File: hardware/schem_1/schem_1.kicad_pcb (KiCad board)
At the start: 2 copper layers, 100 x 40 mm, 68 parts, among them J1 OV7670_Conn_01x24_MountingPin, J2 Micro_SD_Card, J3 USB_B_Mini, J4 Conn_01x03_Female, Q1 NDS332P, SW1 BTN_BOOT, SW2 ESP32_RESET, SW4 DOWN, SW5 UP, SW6 OK, U1 ESP32-S2-WROVER-JC, U2 XC6210B332MR, U5 XC6206-2.8V, U6 XC6206-1.2V, U7 128x32_OLED_SSD1306, U8 MCP23017_SO

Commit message: update footprint for OLED display (no longer using ffc connector)
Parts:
- added R5: 0R DNF, Resistor_SMD:R_0603_1608Metric, F.Cu at (-127.0, -96.1)
- U7: footprint Connector_FFC-FPC:TE_1-1734839-4_1x14-1MP_P0.5mm_Horizontal -> kicad_lib:ER-OLED0.91-7W_SSD1306
- moved C22 458.4 mm to (-259.5, -106.7)
- moved C21 457.4 mm to (-276.3, -46.2)
- moved C17 454.4 mm to (-255.3, -107.0)
- moved C19 446.8 mm to (-247.3, -107.0)
- moved C18 445.1 mm to (-251.3, -107.0)
- moved C20 441.1 mm to (-243.3, -107.0)
- moved R21 441.1 mm to (-239.3, -107.0)
- moved R20 425.2 mm to (-235.3, -107.0)
- moved U7 395.4 mm to (-208.0, -82.0), turned to 90 degrees
- moved C25 380.4 mm to (-239.1, -7.35)
- moved C6 380.4 mm to (-228.2, -23.5)
- moved J2 380.4 mm to (-237.6, -25.3)
- moved R1 380.4 mm to (-228.2, -21.0)
- moved R11 380.4 mm to (-228.2, -18.5)
- moved R12 380.4 mm to (-232.3, -13.4)
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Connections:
- J3 pad 3: Net-(J3-Pad2) -> Net-(J3-Pad3)

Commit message: update footprints for 24way connector, 3D models. add new connector to connect the two PCB's
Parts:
- added H1: MountingHole, MountingHole:MountingHole_2mm, F.Cu at (119.6, 27.0)
- added H2: MountingHole, MountingHole:MountingHole_2mm, F.Cu at (147.6, 27.0)
- added H3: MountingHole, MountingHole:MountingHole_2mm, F.Cu at (147.6, -0.96)
- added H4: MountingHole, MountingHole:MountingHole_2mm, F.Cu at (119.6, -0.96)
- added J5: UJ2-MBH-1-SMT, UJ2-MBH-1-SMT:CUI_UJ2-MBH-1-SMT, F.Cu at (93.1, 4.74)
- added R10: 3.3k, Resistor_SMD:R_0603_1608Metric, F.Cu at (64.0, 15.9)
- added R28: 3.3k, Resistor_SMD:R_0603_1608Metric, F.Cu at (64.0, 31.6)
- added R29: 3.3k, Resistor_SMD:R_0603_1608Metric, F.Cu at (64.0, 27.6)
- added R9: 3.3k, Resistor_SMD:R_0603_1608Metric, F.Cu at (64.0, 19.9)
- C10, C11, C12, C15, C16, C17, C18, C19, C2, C20, C21, C22, C23, C24, C3, C4, C5, C8, C9, D1, D2, D3, D4, J4, R1, R16, R17, R18, R19, R20, R21, R22, R23, R24, R25, R3, R4, R6, R7, U2, U6, U8: moved to B.Cu
- J3: value USB_B_Mini -> PCB_CONNECTOR; footprint kicad_lib:USB_Mini_B_Female_UJ2-MBH-1-SMT-TR-JC -> Connector_FFC-FPC:TE_2-1734839-4_1x24-1MP_P0.5mm_Horizontal; moved to B.Cu
- R26, R27: value 10k -> 3.3k
- R5: value 0R DNF -> 0R; moved to B.Cu
- SW1: footprint Digikey:Switch_Tactile_SMD_4.5x4.5mm_TL3315NF160Q -> kicad_lib:JC_Switch_TL6330
- SW2: footprint Digikey:Switch_Tactile_SMD_4.5x4.5mm_TL3315NF160Q -> kicad_lib:JC_Switch_TL6330; moved to B.Cu
- SW4, SW5, SW6: footprint Digikey:Switch_Tactile_SMD_6x6mm_PTS645 -> kicad_lib:JC_Switch_TL6330
- moved SW2 408.4 mm to (166.6, -5.65), turned to 180 degrees
- moved U1 397.6 mm to (134.9, 11.5), turned to 180 degrees
- moved R2 396.5 mm to (171.7, -0.57)
- moved SW1 396.3 mm to (168.8, -6.03)
- moved C6 392.3 mm to (163.5, -1.33)
- moved C26 390.7 mm to (147.1, 18.5)
- moved R27 390.6 mm to (147.1, 12.0), turned to 180 degrees
- moved R8 388.7 mm to (163.8, 1.97)
- moved C25 387.1 mm to (147.1, 20.1)
- moved C15 363.9 mm to (208.7, 20.1), turned to 270 degrees
- moved C21 362.6 mm to (82.9, 2.95), turned to 90 degrees
- moved C1 362.5 mm to (147.3, 21.9)
- moved U6 359.1 mm to (206.2, 8.60)
- moved J1 357.6 mm to (119.0, 11.0), turned to 90 degrees
- moved C22 357.2 mm to (73.1, 23.5)
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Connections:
- J3 pad 1: /GPIO Expander/Vusb -> Net-(J3-Pad1)
- J3 pad 5: GND -> Net-(J3-Pad5)
- J3 pad 6: GND -> Net-(J3-Pad6)
- R5 pad 1: Net-(J3-Pad2) -> Net-(J5-Pad2)
- R5 pad 2: Net-(J3-Pad3) -> Net-(J5-Pad3)
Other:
- board size 100 x 40 mm -> 80.4 x 34.2 mm

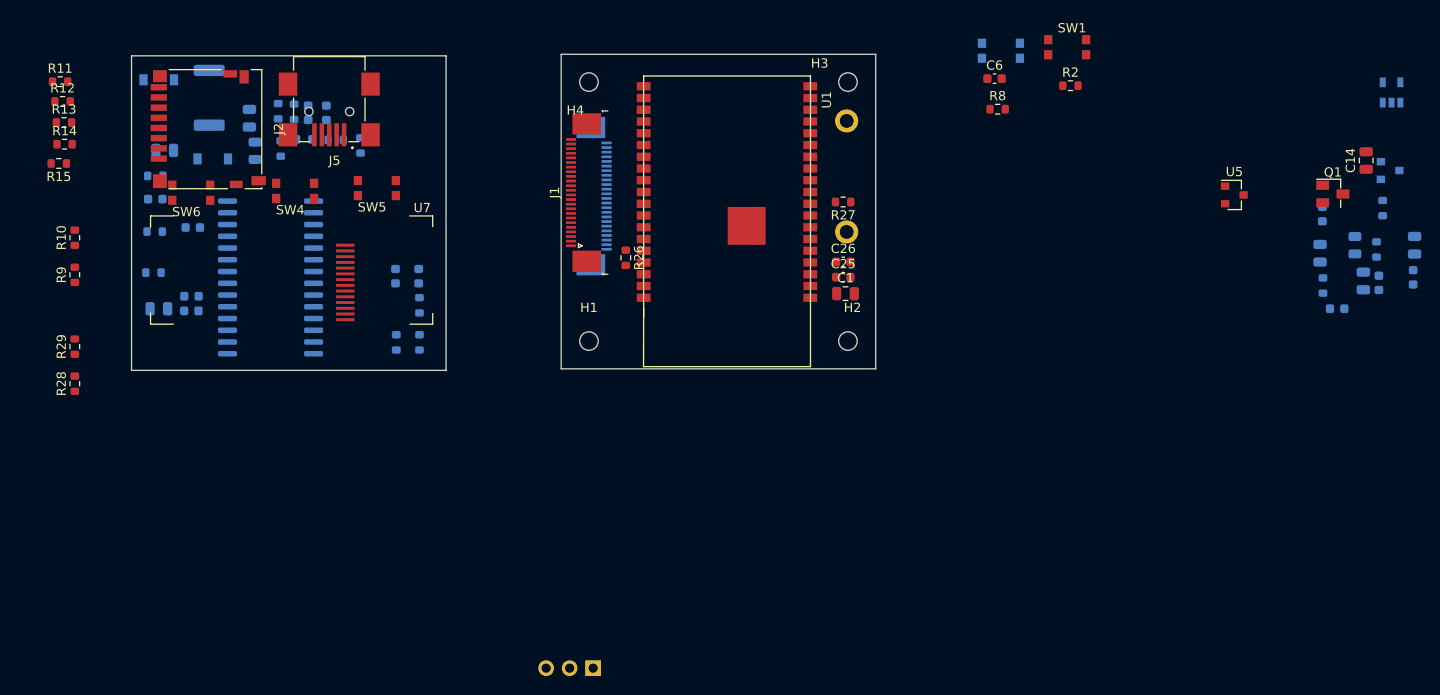
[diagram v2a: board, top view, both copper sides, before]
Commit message: add correct 3d model for esp32 wrover e. initial placement of components done for both boards. need to start routing
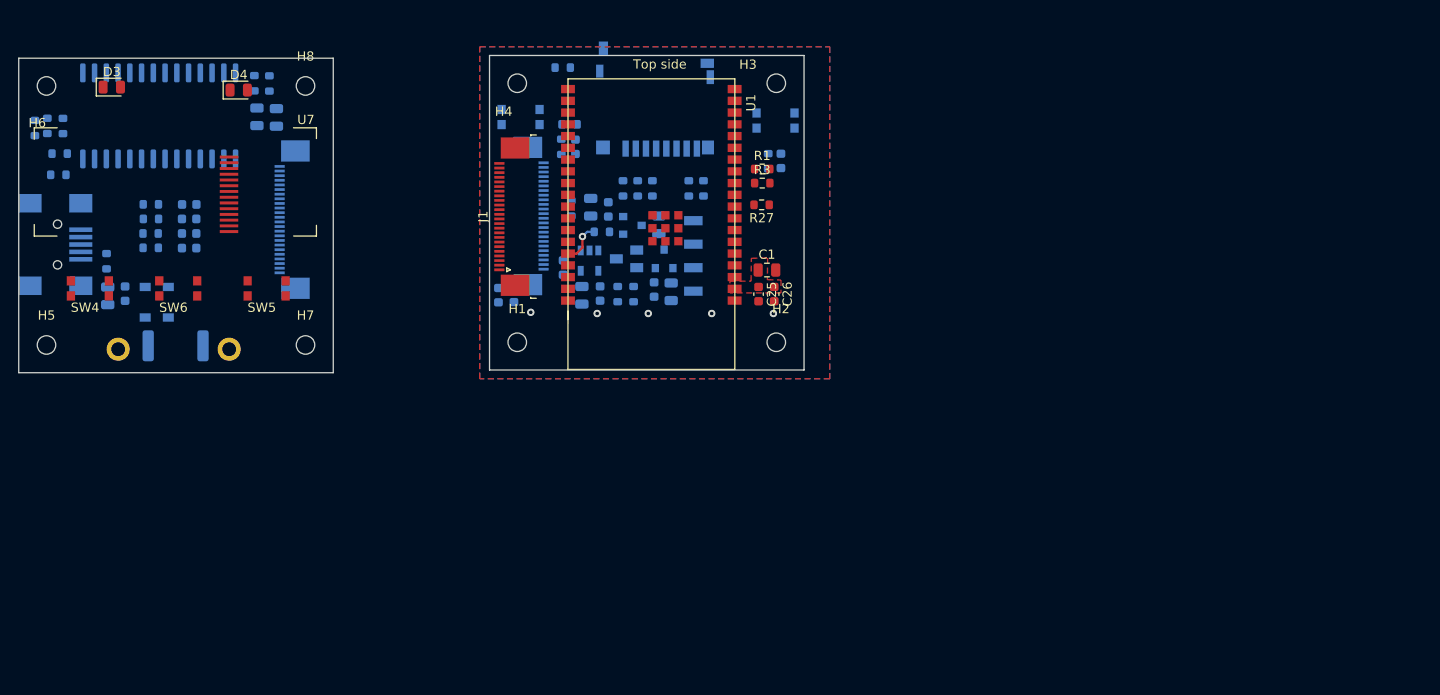
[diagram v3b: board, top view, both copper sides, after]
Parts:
- added H5: MountingHole, MountingHole:MountingHole_2mm, F.Cu at (61.0, 27.5)
- added H6: MountingHole, MountingHole:MountingHole_2mm, F.Cu at (61.0, -0.54)
- added H7: MountingHole, MountingHole:MountingHole_2mm, F.Cu at (89.0, 27.5)
- added H8: MountingHole, MountingHole:MountingHole_2mm, F.Cu at (89.0, -0.54)
- added J6: BACK_PCB_CONNECTOR, Connector_FFC-FPC:TE_2-1734839-4_1x24-1MP_P0.5mm_Horizontal, B.Cu at (87.5, 13.9)
- C14, C6, J2, J5, Q1, R10, R11, R12, R13, R14, R15, R2, R26, R28, R29, R8, R9, SW1, U5: moved to B.Cu
- D3, D4, R1, R3: moved to F.Cu
- J3: value PCB_CONNECTOR -> FRONT_PCB_CONNECTOR
- J4: value Conn_01x03_Female -> BG300-04-X-X-A_REVC; footprint Connector_PinSocket_2.54mm:PinSocket_1x03_P2.54mm_Horizontal -> BG300-04-X-X-A_REVC:GCT_BG300-04-X-X-A_REVC
- U1: value ESP32-S2-WROVER-JC -> ESP32-WROVER-E-JC; footprint kicad_lib:ESP32-S2-WROVER_JC -> kicad_lib:ESP32-WROVER-E-JC
- moved R16 144.3 mm to (61.1, 3.77), turned to 270 degrees
- moved D3 135.5 mm to (68.0, -0.42), turned to 0 degrees
- moved U2 88.6 mm to (119.7, 18.3), turned to 270 degrees
- moved C8 84.5 mm to (118.8, 22.1)
- moved C24 84.2 mm to (120.8, 21.9), turned to 270 degrees
- moved C12 83.8 mm to (116.8, 19.1), turned to 270 degrees
- moved R17 83.2 mm to (122.7, 22.0), turned to 270 degrees
- moved C15 82.1 mm to (126.6, 21.5)
- moved C16 81.7 mm to (127.2, 14.5)
- moved U6 79.1 mm to (127.7, 18.1), turned to 90 degrees
- moved C10 79.0 mm to (119.8, 12.6)
- moved C11 77.2 mm to (121.7, 12.8)
- moved Q1 76.7 mm to (123.7, 18.1), turned to 180 degrees
- moved C14 76.5 mm to (128.5, 21.7), turned to 270 degrees
- moved R19 74.5 mm to (124.4, 22.0)
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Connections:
- C12 pad 1: /GPIO Expander/Vusb -> /5V_USB_SC
- C23 pad 1: /GPIO Expander/Vusb -> /5V_USB_SC
- C9 pad 1: /GPIO Expander/Vusb -> /5V_USB_SC
- D1 pad 1: /GPIO Expander/Vusb -> /5V_USB_SC
- D2 pad 2: /GPIO Expander/Vusb -> /5V_USB_SC
- J3 pad 1: Net-(J3-Pad1) -> GND
- J3 pad 10: Net-(J3-Pad10) -> GND
- J3 pad 11: Net-(J3-Pad11) -> /SCL
- J3 pad 12: Net-(J3-Pad12) -> GND
- J3 pad 13: Net-(J3-Pad13) -> GND
- J3 pad 14: Net-(J3-Pad14) -> /SDA
- J3 pad 15: Net-(J3-Pad15) -> GND
- J3 pad 16: Net-(J3-Pad16) -> GND
- J3 pad 17: Net-(J3-Pad17) -> /CAM_PWR
- J3 pad 18: Net-(J3-Pad18) -> GND
- J3 pad 19: Net-(J3-Pad19) -> GND
- J3 pad 2: Net-(J3-Pad2) -> GND
- J3 pad 20: Net-(J3-Pad20) -> GND
- J3 pad 21: Net-(J3-Pad21) -> GND
- J3 pad 22: Net-(J3-Pad22) -> GND
- J3 pad 23: Net-(J3-Pad23) -> GND
- J3 pad 24: Net-(J3-Pad24) -> GND
- J3 pad 3: Net-(J3-Pad3) -> /5V_USB_SC
- J3 pad 4: Net-(J3-Pad4) -> /5V_USB_SC
- J3 pad 5: Net-(J3-Pad5) -> GND
- J3 pad 6: Net-(J3-Pad6) -> GND
- J3 pad 7: Net-(J3-Pad7) -> +3V3
- J3 pad 8: Net-(J3-Pad8) -> +3V3
- J3 pad 9: Net-(J3-Pad9) -> GND
- J5 pad 1: /GPIO Expander/Vusb -> /5V_USB_SC
- R22 pad 1: /GPIO Expander/Vusb -> /5V_USB_SC
- U2 pad 1: /GPIO Expander/Vusb -> /5V_USB_SC
- U2 pad 3: /GPIO Expander/Vusb -> /5V_USB_SC
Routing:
- net /SCL: track 0.00 -> 4.51 mm, vias 0 -> 1
- net GND: vias 0 -> 5
- added copper zone on F.Cu, net +3V3
- added copper zone on B.Cu, net GND
- added copper zone on F.Cu, net GND
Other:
- board size 80.4 x 34.2 mm -> 84.9 x 34.3 mm
- copper layers 2 -> 4
- net class 5V added: clearance 0.3, trace_width 0.3, via_dia 0.8, via_drill 0.4
- rule pad_to_mask_clearance: 0 -> 0.0025
- board text added: "1 GND"
- board text added: "Top side"

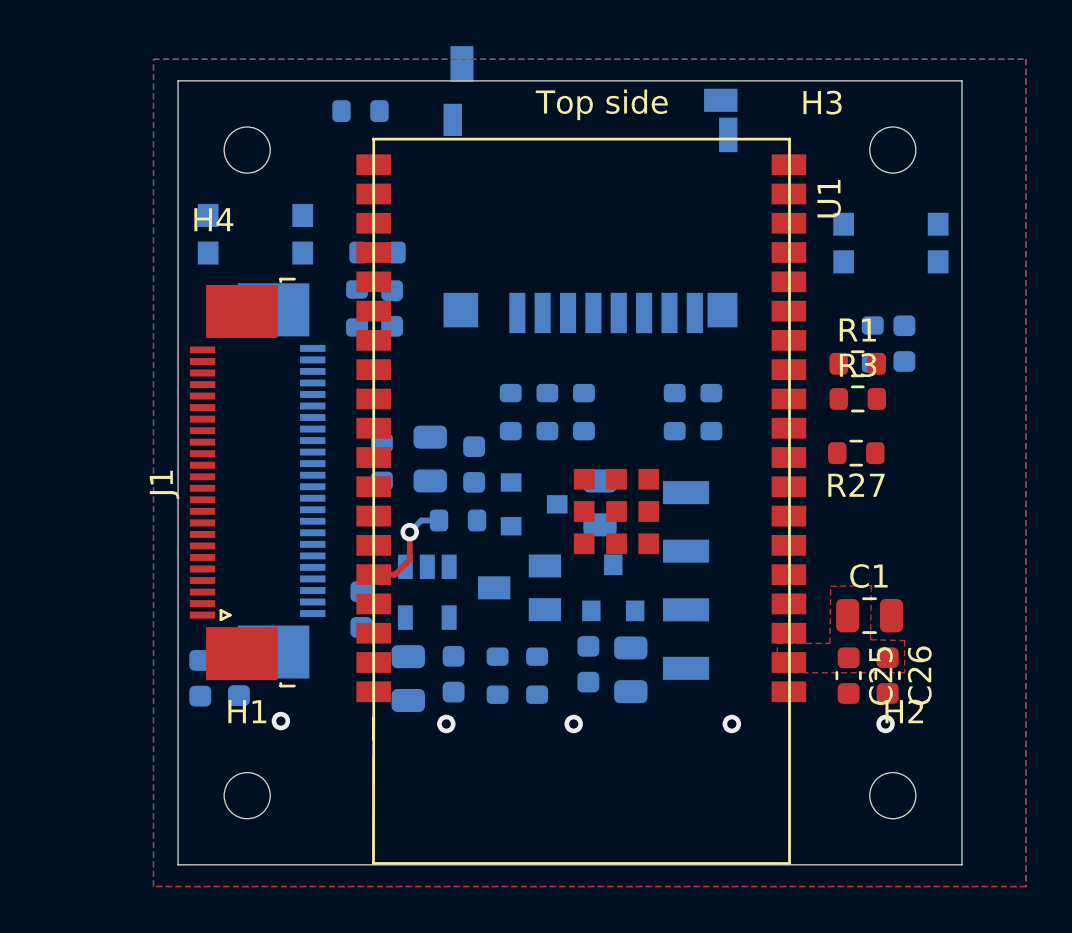
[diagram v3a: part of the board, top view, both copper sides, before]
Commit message: lay tracks and zones for front pcb.
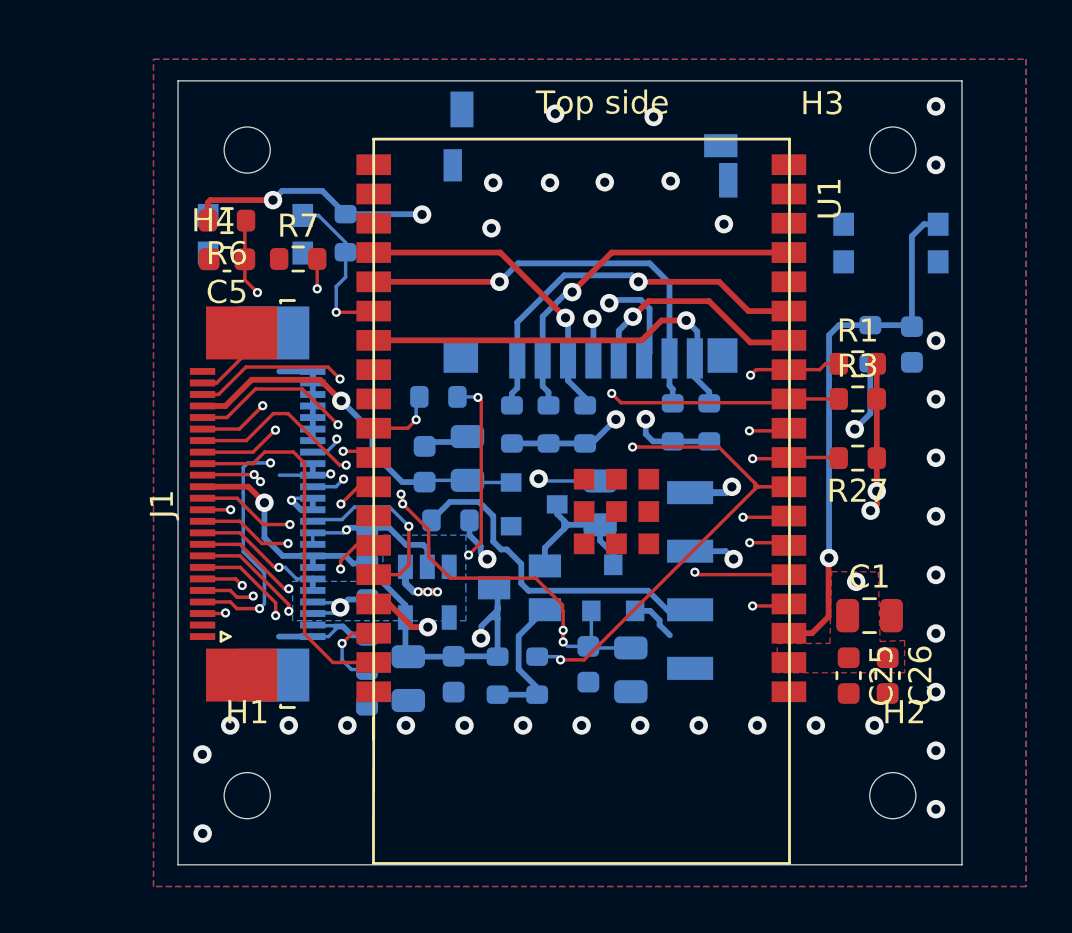
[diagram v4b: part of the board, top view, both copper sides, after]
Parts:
- C5, R6, R7: moved to F.Cu
- moved C4 9.25 mm to (117.1, 16.3), turned to 270 degrees
- moved C5 7.47 mm to (111.0, 3.90), turned to 180 degrees
- moved R7 6.96 mm to (114.1, 3.89), turned to 0 degrees
- moved R6 6.81 mm to (111.0, 2.22), turned to 180 degrees
- moved C3 5.57 mm to (117.0, 22.5)
- moved R4 3.74 mm to (120.1, 9.87), turned to 180 degrees
- moved C11 2.15 mm to (119.5, 12.8)
- moved J2 1.97 mm to (126.7, 2.85)
- moved R2 1.62 mm to (116.1, 2.77), turned to 270 degrees
- moved C10 1.61 mm to (121.4, 12.5)
- moved J3 1.00 mm to (113.3, 14.5)
- moved J1 0.93 mm to (111.3, 14.5)
- moved R13 0.54 mm to (126.5, 11.1)
- moved R11 0.54 mm to (123.3, 11.1)
- moved R12 0.54 mm to (124.9, 11.1)
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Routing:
- net +3V3: track 0.04 -> 56.9 mm, vias 0 -> 12
- net GND: track 0.00 -> 45.2 mm, vias 5 -> 39
- net /CAM_PWR: track 0.00 -> 34.8 mm, vias 0 -> 3
- net /TWI_SCK: track 0.00 -> 30.2 mm, vias 0 -> 2
- net /CSI_D4: track 0.00 -> 30.2 mm, vias 0 -> 2
- net /TWI_SDA: track 0.00 -> 28.8 mm, vias 0 -> 2
- net /CSI_VSYNC: track 0.00 -> 27.6 mm, vias 0 -> 2
- net /CSI_D5: track 0.00 -> 26.6 mm, vias 0 -> 2
- net +1V2: track 0.00 -> 26.4 mm, vias 0 -> 6
- net /CSI_D7: track 0.00 -> 26.2 mm, vias 0 -> 2
- net /CSI_D6: track 0.00 -> 25.9 mm, vias 0 -> 2
- net /5V_USB_SC: track 0.00 -> 23.6 mm, vias 0 -> 5
- net /SDA: track 0.00 -> 23.5 mm, vias 0 -> 2
- net /ESP32_RST: track 0.00 -> 23.3 mm, vias 0 -> 1
- net Net-(J1-Pad6): track 0.00 -> 20.2 mm, vias 0 -> 3
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- added copper zone on In1.Cu, net +3V3
- added copper zone on B.Cu, net /5V_USB_SC
- added copper zone on In1.Cu, net /5V_USB_SC
- added copper zone on In1.Cu, net GND
- added copper zone on In2.Cu, net GND
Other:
- rule trace_min: 0.2 -> 0.15
- rule via_min_drill: 0.3 -> 0.2

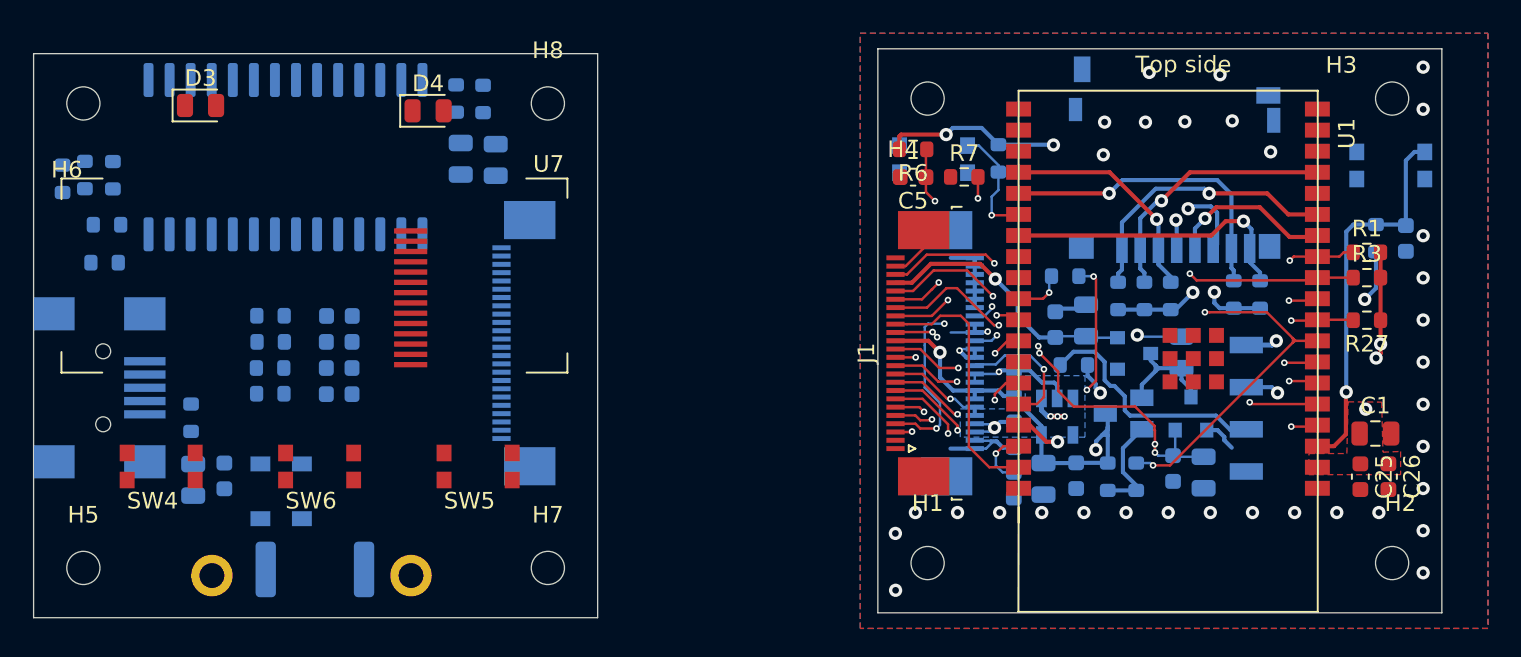
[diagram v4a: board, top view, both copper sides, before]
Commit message: finish first round tracks and filled zones for front PCB. Do silk screen
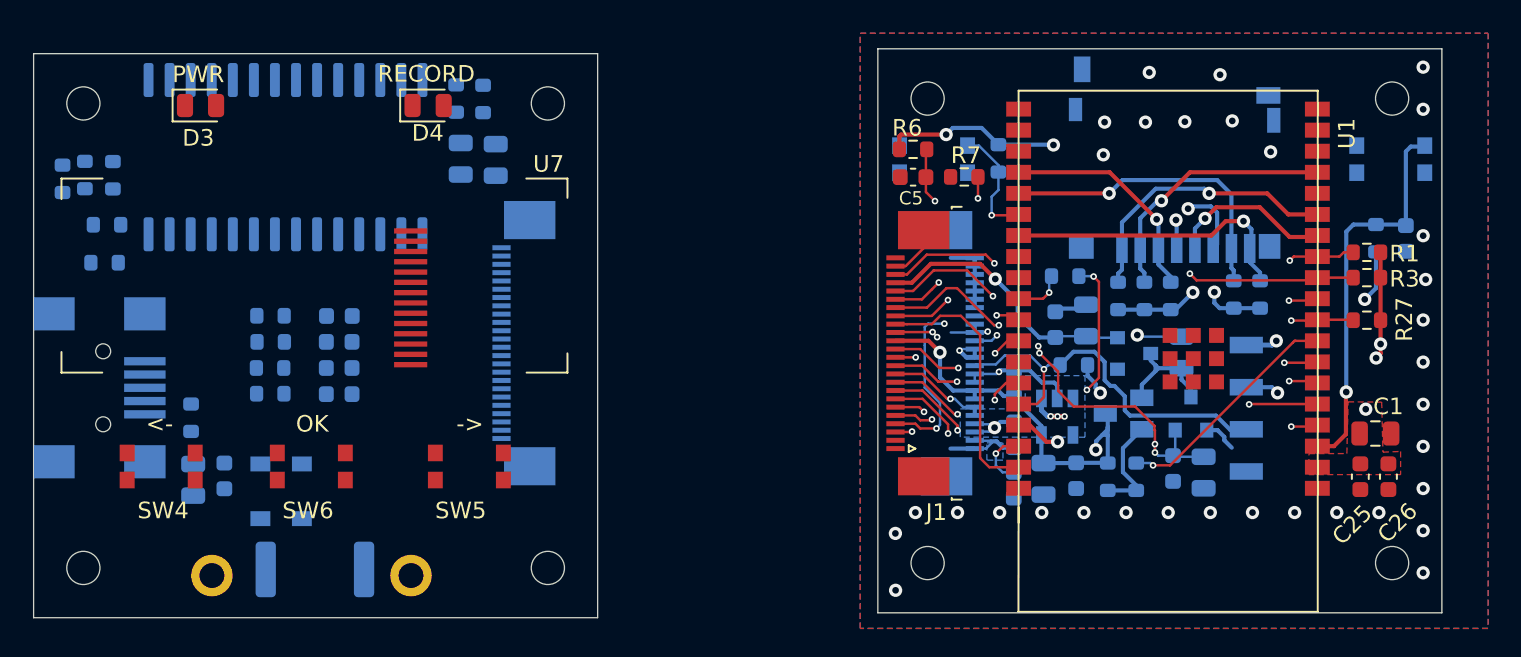
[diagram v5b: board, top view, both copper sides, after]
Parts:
- moved SW5 0.53 mm to (86.7, 22.6)
- moved SW6 0.50 mm to (77.2, 22.6)
- moved SW2 0.38 mm to (142.3, 1.51)
- moved D4 0.32 mm to (81.7, -0.42)
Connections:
- J3 pad 17: /CAM_PWR -> GND
- J6 pad 8: /CAM_PWR -> GND
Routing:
- net /CAM_PWR: track 34.8 -> 14.1 mm, vias 3 -> 1
- net /SCL: track 22.8 -> 23.9 mm
- net /CSI_D4: track 30.2 -> 29.1 mm
- net /U0TXD: track 19.3 -> 19.8 mm
- added copper zone on B.Cu, net /CSI_PCLK
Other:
- board text added: "->"
- board text added: "<-"
- board text added: "BOOT"
- board text added: "Back PCB (with LCD) Contains the following: - OLED SCREEN - USB 5V IN - SUPERCAPACITOR + CHARGE CIRCUIT - I2C IO EXPANDER - 3 BUTTONS - LED (RECORDING) - LED (POWER)"
- board text added: "Front PCB (with Camera) Contains the following: - ESP32 WROVER - OV7670 CAMERA MODULE - BOOT/RESET SWITCHES FOR ESP32 - 3V3 LDO - 2.8V LDO - 1.2V LDO - SD CARD - UART CONNECTOR"
- board text added: "OK"
- board text added: "PWR"
- board text added: "RECORD"
- board text added: "RESET"
